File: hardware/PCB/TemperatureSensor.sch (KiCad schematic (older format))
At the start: 2 parts, among them IC1 BQ24092DGQR, IC2 ESP32-D0WD-V3

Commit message: Add new sensors to board
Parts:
- added IC3: SHT31-ARP-B2.5kS, SON50P250X250X100-9N-D, symbol ProjectLibrary:SHT31-ARP-B2.5kS
- added U1: LTR-329ALS-01, LTR329ALS01, symbol ProjectLibrary:LTR-329ALS-01
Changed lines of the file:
@@
+	1    0    0    -1
+$EndComp
+$Comp
+L ProjectLibrary:SHT31-ARP-B2.5kS IC3
+U 1 1 5FBA3C37
+P 4400 4050
+F 0 "IC3" H 5000 4315 50  0000 C CNN
+F 1 "SHT31-ARP-B2.5kS" H 5000 4224 50  0000 C CNN
+F 2 "SON50P250X250X100-9N-D" H 5450 4150 50  0001 L CNN
+F 3 "https://componentsearchengine.com/Datasheets/1/SHT31-ARP-B2.5kS.pdf" H 5450 4050 50  0001 L CNN
+F 4 "Board Mount Humidity Sensors +/- 2%RH 14 bit Resolution" H 5450 3950 50  0001 L CNN "Description"
+F 5 "1" H 5450 3850 50  0001 L CNN "Height"
+F 6 "403-SHT31-ARP-B" H 5450 3750 50  0001 L CNN "Mouser Part Number"
+F 7 "https://www.mouser.co.uk/ProductDetail/Sensirion/SHT31-ARP-B25kS?qs=y6ZabgHbY%252BxqV2K0yYcGiA%3D%3D" H 5450 3650 50  0001 L CNN "Mouser Price/Stock"
+F 8 "Sensirion" H 5450 3550 50  0001 L CNN "Manufacturer_Name"
+F 9 "SHT31-ARP-B2.5kS" H 5450 3450 50  0001 L CNN "Manufacturer_Part_Number"
+	1    4400 4050
+	1    0    0    -1
+$EndComp
+$Comp
+L ProjectLibrary:LTR-329ALS-01 U1
+U 1 1 5FBA3CE3
+P 8950 4350
+F 0 "U1" H 9450 4615 50  0000 C CNN
+F 1 "LTR-329ALS-01" H 9450 4524 50  0000 C CNN
+F 2 "LTR329ALS01" H 9800 4450 50  0001 L CNN
+F 3 "" H 9800 4350 50  0001 L CNN
+F 4 "Ambient Light Sensors Ambient Light Photo Sensor" H 9800 4250 50  0001 L CNN "Description"
+F 5 "0" H 9800 4150 50  0001 L CNN "Height"
+F 6 "859-LTR-329ALS-01" H 9800 4050 50  0001 L CNN "Mouser Part Number"
+F 7 "https://www.mouser.co.uk/ProductDetail/Lite-On/LTR-329ALS-01?qs=Ml%2FaxAEbwm8eHg8LIDPUrw%3D%3D" H 9800 3950 50  0001 L CNN "Mouser Price/Stock"
+F 8 "Lite-On" H 9800 3850 50  0001 L CNN "Manufacturer_Name"
+F 9 "LTR-329ALS-01" H 9800 3750 50  0001 L CNN "Manufacturer_Part_Number"
+	1    8950 4350
 	1    0    0    -1
 $EndComp

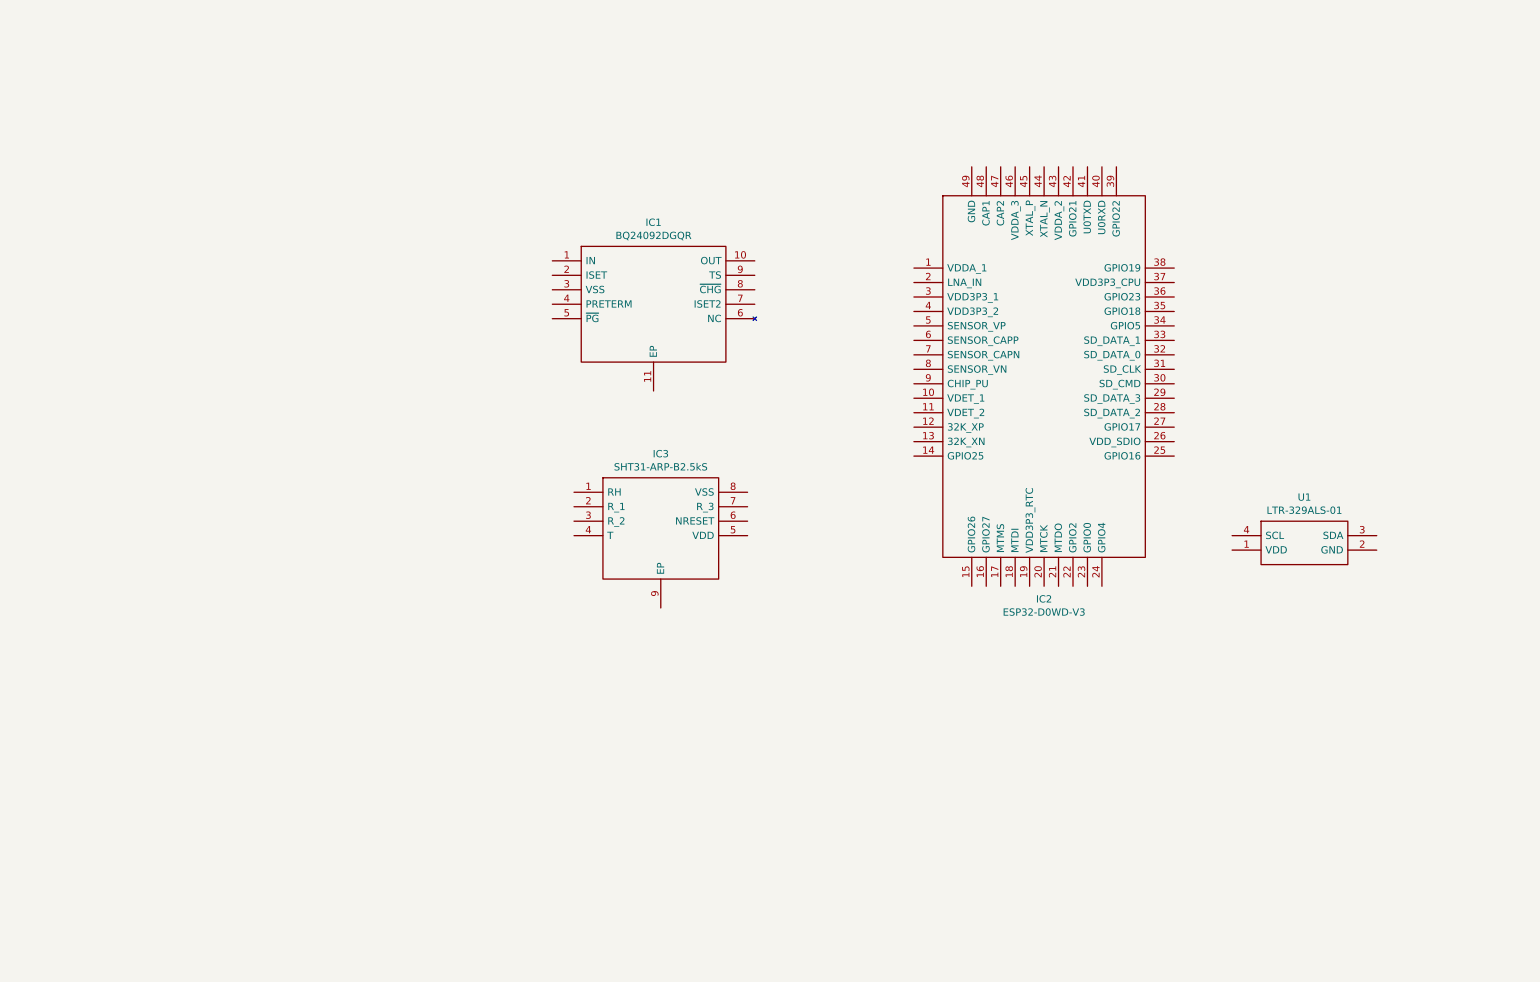
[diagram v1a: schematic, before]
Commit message: add usb and ftdi circuit
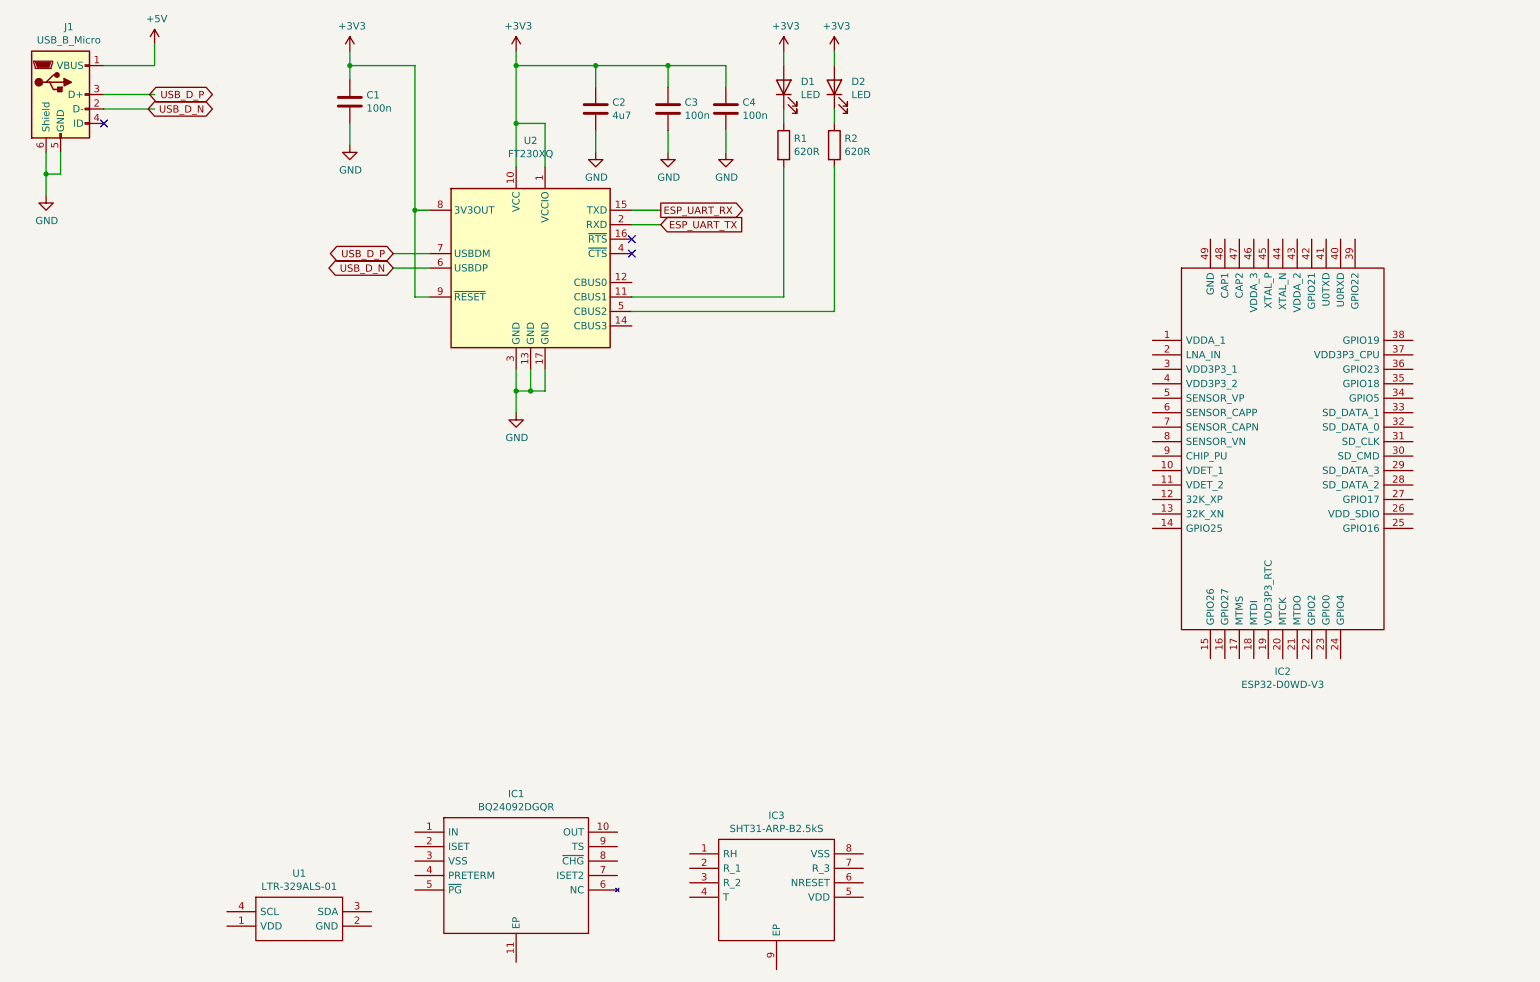
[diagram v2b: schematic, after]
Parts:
- added C1, C3, C4: 100n, Capacitor_SMD:C_0603_1608Metric, symbol Device:C
- added C2: 4u7, Capacitor_SMD:C_0603_1608Metric, symbol Device:C
- added D1, D2: LED, LED_SMD:LED_0603_1608Metric, symbol Device:LED
- added J1: USB_B_Micro, Connector_USB:USB_Micro-B_Amphenol_10118194_Horizontal, symbol Connector:USB_B_Micro
- added R1, R2: 620R, Resistor_SMD:R_0603_1608Metric, symbol Device:R
- added U2: FT230XQ, Package_DFN_QFN:QFN-16-1EP_4x4mm_P0.65mm_EP2.1x2.1mm, symbol Interface_USB:FT230XQ
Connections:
- net labels added: +3V3, +5V, ESP_UART_RX, ESP_UART_TX, GND, USB_D_N, USB_D_P
- wire segments 0 -> 48
- no-connect marks 0 -> 3
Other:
- moved on the sheet: IC1, IC2, IC3, U1

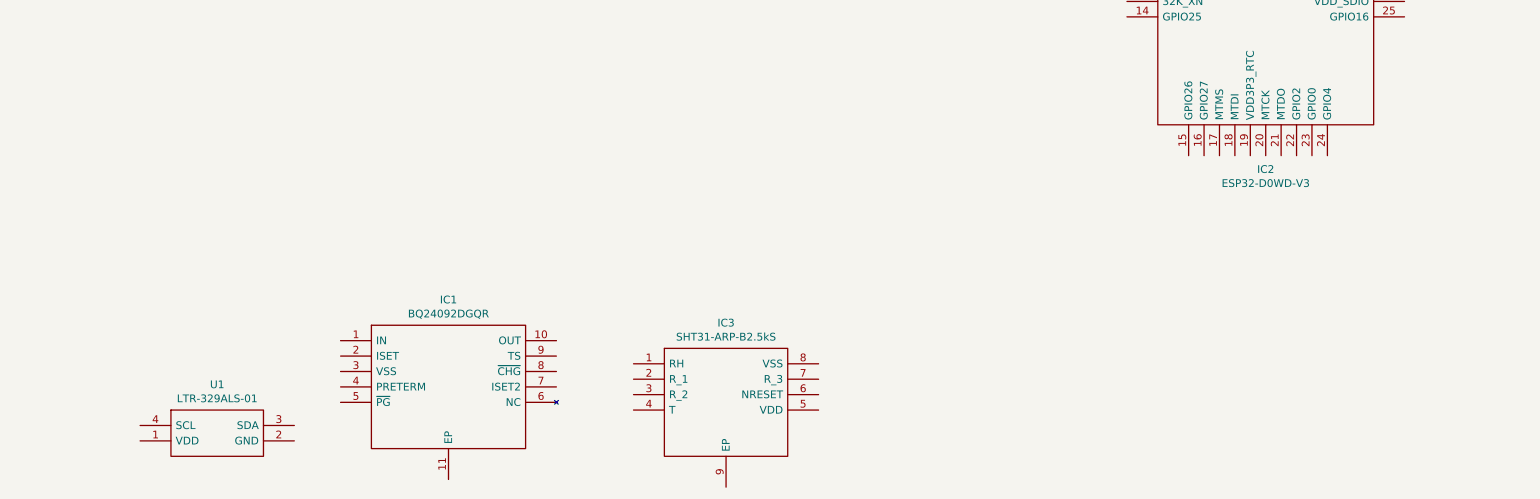
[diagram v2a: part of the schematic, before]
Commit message: started display circuit
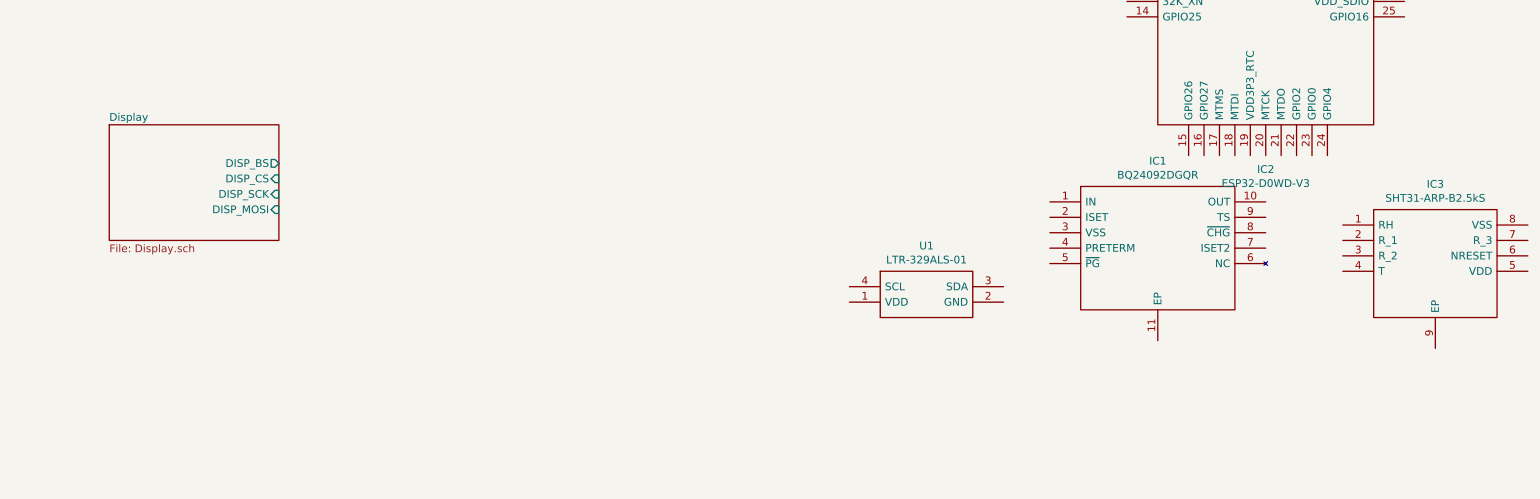
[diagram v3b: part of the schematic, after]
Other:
- moved on the sheet: IC1, IC3, U1
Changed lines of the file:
@@
 $Descr A4 11693 8268
 encoding utf-8
-Sheet 1 1
+Sheet 1 2
 Title ""
 Date ""
@@
 L ProjectLibrary:BQ24092DGQR IC1
 U 1 1 5FB42655
-P 3300 6400
-F 0 "IC1" H 4000 6665 50  0000 C CNN
-F 1 "BQ24092DGQR" H 4000 6574 50  0000 C CNN
-F 2 "SOP50P490X110-11N" H 4550 6500 50  0001 L CNN
-F 3 "http://www.ti.com/lit/gpn/BQ24092" H 4550 6400 50  0001 L CNN
-F 4 "1A, Single-Input, Single-Cell Li-Ion Battery Charger with Operation Over JEITA and 10k NTC" H 4550 6300 50  0001 L CNN "Description"
-F 5 "1.1" H 4550 6200 50  0001 L CNN "Height"
-F 6 "595-BQ24092DGQR" H 4550 6100 50  0001 L CNN "Mouser Part Number"
-F 7 "https://www.mouser.co.uk/ProductDetail/Texas-Instruments/BQ24092DGQR?qs=C44r%252BX3hXgKGrpCEuObqhg%3D%3D" H 4550 6000 50  0001 L CNN "Mouser Price/Stock"
-F 8 "Texas Instruments" H 4550 5900 50  0001 L CNN "Manufacturer_Name"
-F 9 "BQ24092DGQR" H 4550 5800 50  0001 L CNN "Manufacturer_Part_Number"
-	1    3300 6400
+P 7900 5500
+F 0 "IC1" H 8600 5765 50  0000 C CNN
+F 1 "BQ24092DGQR" H 8600 5674 50  0000 C CNN
+F 2 "SOP50P490X110-11N" H 9150 5600 50  0001 L CNN
+F 3 "http://www.ti.com/lit/gpn/BQ24092" H 9150 5500 50  0001 L CNN
+F 4 "1A, Single-Input, Single-Cell Li-Ion Battery Charger with Operation Over JEITA and 10k NTC" H 9150 5400 50  0001 L CNN "Description"
+F 5 "1.1" H 9150 5300 50  0001 L CNN "Height"
+F 6 "595-BQ24092DGQR" H 9150 5200 50  0001 L CNN "Mouser Part Number"
+F 7 "https://www.mouser.co.uk/ProductDetail/Texas-Instruments/BQ24092DGQR?qs=C44r%252BX3hXgKGrpCEuObqhg%3D%3D" H 9150 5100 50  0001 L CNN "Mouser Price/Stock"
+F 8 "Texas Instruments" H 9150 5000 50  0001 L CNN "Manufacturer_Name"
+F 9 "BQ24092DGQR" H 9150 4900 50  0001 L CNN "Manufacturer_Part_Number"
+	1    7900 5500
 	1    0    0    -1
 $EndComp
@@
 L ProjectLibrary:SHT31-ARP-B2.5kS IC3
 U 1 1 5FBA3C37
-P 5200 6550
-F 0 "IC3" H 5800 6815 50  0000 C CNN
-F 1 "SHT31-ARP-B2.5kS" H 5800 6724 50  0000 C CNN
-F 2 "SON50P250X250X100-9N-D" H 6250 6650 50  0001 L CNN
-F 3 "https://componentsearchengine.com/Datasheets/1/SHT31-ARP-B2.5kS.pdf" H 6250 6550 50  0001 L CNN
-F 4 "Board Mount Humidity Sensors +/- 2%RH 14 bit Resolution" H 6250 6450 50  0001 L CNN "Description"
-F 5 "1" H 6250 6350 50  0001 L CNN "Height"
-F 6 "403-SHT31-ARP-B" H 6250 6250 50  0001 L CNN "Mouser Part Number"
-F 7 "https://www.mouser.co.uk/ProductDetail/Sensirion/SHT31-ARP-B25kS?qs=y6ZabgHbY%252BxqV2K0yYcGiA%3D%3D" H 6250 6150 50  0001 L CNN "Mouser Price/Stock"
-F 8 "Sensirion" H 6250 6050 50  0001 L CNN "Manufacturer_Name"
-F 9 "SHT31-ARP-B2.5kS" H 6250 5950 50  0001 L CNN "Manufacturer_Part_Number"
-	1    5200 6550
+P 9800 5650
+F 0 "IC3" H 10400 5915 50  0000 C CNN
+F 1 "SHT31-ARP-B2.5kS" H 10400 5824 50  0000 C CNN
+F 2 "SON50P250X250X100-9N-D" H 10850 5750 50  0001 L CNN
+F 3 "https://componentsearchengine.com/Datasheets/1/SHT31-ARP-B2.5kS.pdf" H 10850 5650 50  0001 L CNN
+F 4 "Board Mount Humidity Sensors +/- 2%RH 14 bit Resolution" H 10850 5550 50  0001 L CNN "Description"
+F 5 "1" H 10850 5450 50  0001 L CNN "Height"
+F 6 "403-SHT31-ARP-B" H 10850 5350 50  0001 L CNN "Mouser Part Number"
+F 7 "https://www.mouser.co.uk/ProductDetail/Sensirion/SHT31-ARP-B25kS?qs=y6ZabgHbY%252BxqV2K0yYcGiA%3D%3D" H 10850 5250 50  0001 L CNN "Mouser Price/Stock"
+F 8 "Sensirion" H 10850 5150 50  0001 L CNN "Manufacturer_Name"
+F 9 "SHT31-ARP-B2.5kS" H 10850 5050 50  0001 L CNN "Manufacturer_Part_Number"
+	1    9800 5650
 	1    0    0    -1
 $EndComp
@@
 L ProjectLibrary:LTR-329ALS-01 U1
 U 1 1 5FBA3CE3
-P 2000 6950
-F 0 "U1" H 2500 7215 50  0000 C CNN
-F 1 "LTR-329ALS-01" H 2500 7124 50  0000 C CNN
-F 2 "LTR329ALS01" H 2850 7050 50  0001 L CNN
-F 3 "" H 2850 6950 50  0001 L CNN
-F 4 "Ambient Light Sensors Ambient Light Photo Sensor" H 2850 6850 50  0001 L CNN "Description"
-F 5 "0" H 2850 6750 50  0001 L CNN "Height"
-F 6 "859-LTR-329ALS-01" H 2850 6650 50  0001 L CNN "Mouser Part Number"
-F 7 "https://www.mouser.co.uk/ProductDetail/Lite-On/LTR-329ALS-01?qs=Ml%2FaxAEbwm8eHg8LIDPUrw%3D%3D" H 2850 6550 50  0001 L CNN "Mouser Price/Stock"
-F 8 "Lite-On" H 2850 6450 50  0001 L CNN "Manufacturer_Name"
-F 9 "LTR-329ALS-01" H 2850 6350 50  0001 L CNN "Manufacturer_Part_Number"
-	1    2000 6950
+P 6600 6050
+F 0 "U1" H 7100 6315 50  0000 C CNN
+F 1 "LTR-329ALS-01" H 7100 6224 50  0000 C CNN
+F 2 "LTR329ALS01" H 7450 6150 50  0001 L CNN
+F 3 "" H 7450 6050 50  0001 L CNN
+F 4 "Ambient Light Sensors Ambient Light Photo Sensor" H 7450 5950 50  0001 L CNN "Description"
+F 5 "0" H 7450 5850 50  0001 L CNN "Height"
+F 6 "859-LTR-329ALS-01" H 7450 5750 50  0001 L CNN "Mouser Part Number"
+F 7 "https://www.mouser.co.uk/ProductDetail/Lite-On/LTR-329ALS-01?qs=Ml%2FaxAEbwm8eHg8LIDPUrw%3D%3D" H 7450 5650 50  0001 L CNN "Mouser Price/Stock"
+F 8 "Lite-On" H 7450 5550 50  0001 L CNN "Manufacturer_Name"
+F 9 "LTR-329ALS-01" H 7450 5450 50  0001 L CNN "Manufacturer_Part_Number"
+	1    6600 6050
 	1    0    0    -1
 $EndComp
@@
 Wire Wire Line
 	5850 1500 5850 1400
+$Sheet
+S 1800 5000 1100 750
+U 5FC321F3
+F0 "Display" 50
+F1 "Display.sch" 50
+F2 "DISP_BS" O R 2900 5250 50
+F3 "DISP_CS" I R 2900 5350 50
+F4 "DISP_SCK" I R 2900 5450 50
+F5 "DISP_MOSI" I R 2900 5550 50
+$EndSheet
 $EndSCHEMATC

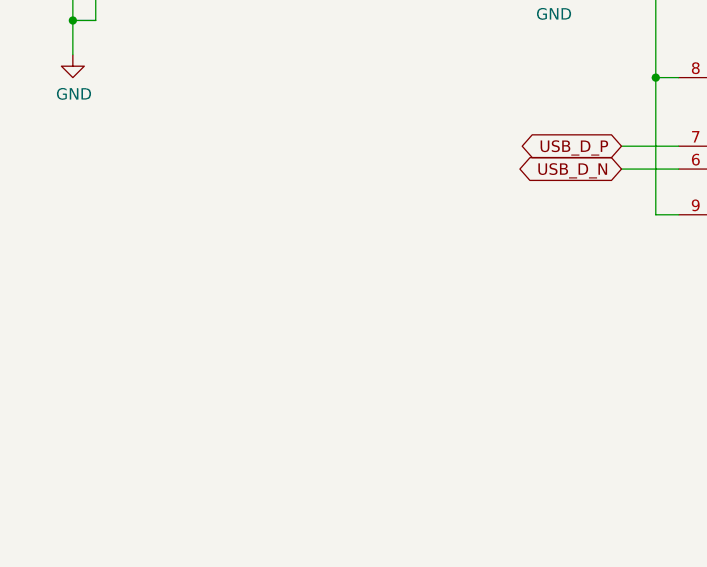
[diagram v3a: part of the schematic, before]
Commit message: Add 4 mounting holes with via pads
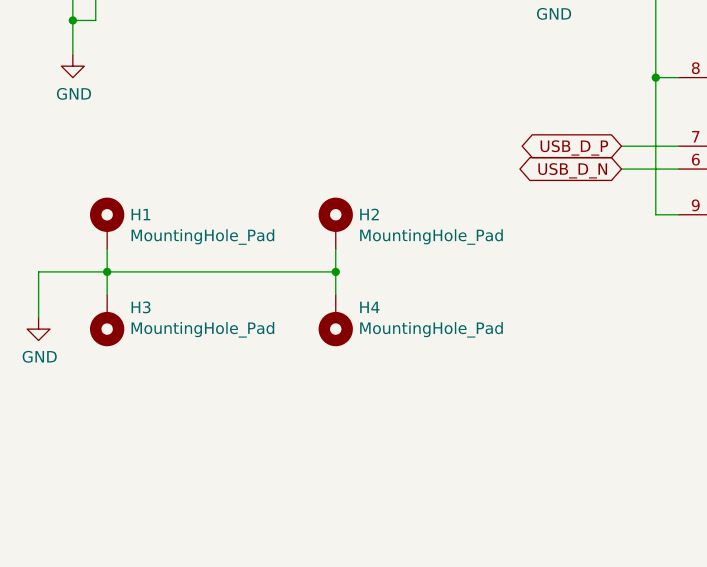
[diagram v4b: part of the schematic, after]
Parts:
- added H1, H2, H3, H4: MountingHole_Pad, MountingHole:MountingHole_2.2mm_M2_Pad_Via, symbol Mechanical:MountingHole_Pad
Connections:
- wire segments 48 -> 55
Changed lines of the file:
@@
 F5 "DISP_MOSI" I R 2900 5550 50
 $EndSheet
+$Comp
+L Mechanical:MountingHole_Pad H1
+U 1 1 5FBE78FD
+P 900 2750
+F 0 "H1" H 1000 2799 50  0000 L CNN
+F 1 "MountingHole_Pad" H 1000 2708 50  0000 L CNN
+F 2 "MountingHole:MountingHole_2.2mm_M2_Pad_Via" H 900 2750 50  0001 C CNN
+F 3 "~" H 900 2750 50  0001 C CNN
+	1    900  2750
+	1    0    0    -1
+$EndComp
+$Comp
+L Mechanical:MountingHole_Pad H2
+U 1 1 5FBEA23E
+P 1900 2750
+F 0 "H2" H 2000 2799 50  0000 L CNN
+F 1 "MountingHole_Pad" H 2000 2708 50  0000 L CNN
+F 2 "MountingHole:MountingHole_2.2mm_M2_Pad_Via" H 1900 2750 50  0001 C CNN
+F 3 "~" H 1900 2750 50  0001 C CNN
+	1    1900 2750
+	1    0    0    -1
+$EndComp
+$Comp
+L Mechanical:MountingHole_Pad H4
+U 1 1 5FBEAEC2
+P 1900 3150
+F 0 "H4" H 1800 3107 50  0000 R CNN
+F 1 "MountingHole_Pad" H 1800 3198 50  0000 R CNN
+F 2 "MountingHole:MountingHole_2.2mm_M2_Pad_Via" H 1900 3150 50  0001 C CNN
+F 3 "~" H 1900 3150 50  0001 C CNN
+	1    1900 3150
+	-1   0    0    1
+$EndComp
+$Comp
+L Mechanical:MountingHole_Pad H3
+U 1 1 5FBE92B5
+P 900 3150
+F 0 "H3" H 800 3107 50  0000 R CNN
+F 1 "MountingHole_Pad" H 800 3198 50  0000 R CNN
+F 2 "MountingHole:MountingHole_2.2mm_M2_Pad_Via" H 900 3150 50  0001 C CNN
+F 3 "~" H 900 3150 50  0001 C CNN
+	1    900  3150
+	-1   0    0    1
+$EndComp
+Wire Wire Line
+	900  3050 900  2950
+Wire Wire Line
+	1900 2850 1900 2950
+Wire Wire Line
+	1900 2950 900  2950
+Connection ~ 1900 2950
+Wire Wire Line
+	1900 2950 1900 3050
+Connection ~ 900  2950
+Wire Wire Line
+	900  2950 900  2850
+Wire Wire Line
+	900  2950 600  2950
+$Comp
+L power:GND #PWR?
+U 1 1 5FBF5B51
+P 600 3150
+F 0 "#PWR?" H 600 2900 50  0001 C CNN
+F 1 "GND" H 605 2977 50  0000 C CNN
+F 2 "" H 600 3150 50  0001 C CNN
+F 3 "" H 600 3150 50  0001 C CNN
+	1    600  3150
+	1    0    0    -1
+$EndComp
+Wire Wire Line
+	600  2950 600  3150
 $EndSCHEMATC
